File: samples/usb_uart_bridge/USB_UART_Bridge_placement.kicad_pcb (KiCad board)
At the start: 2 copper layers, 68 x 73 mm, 5 parts, among them J1 USB-C, U1 TLV75518, U2 CYUSB3014

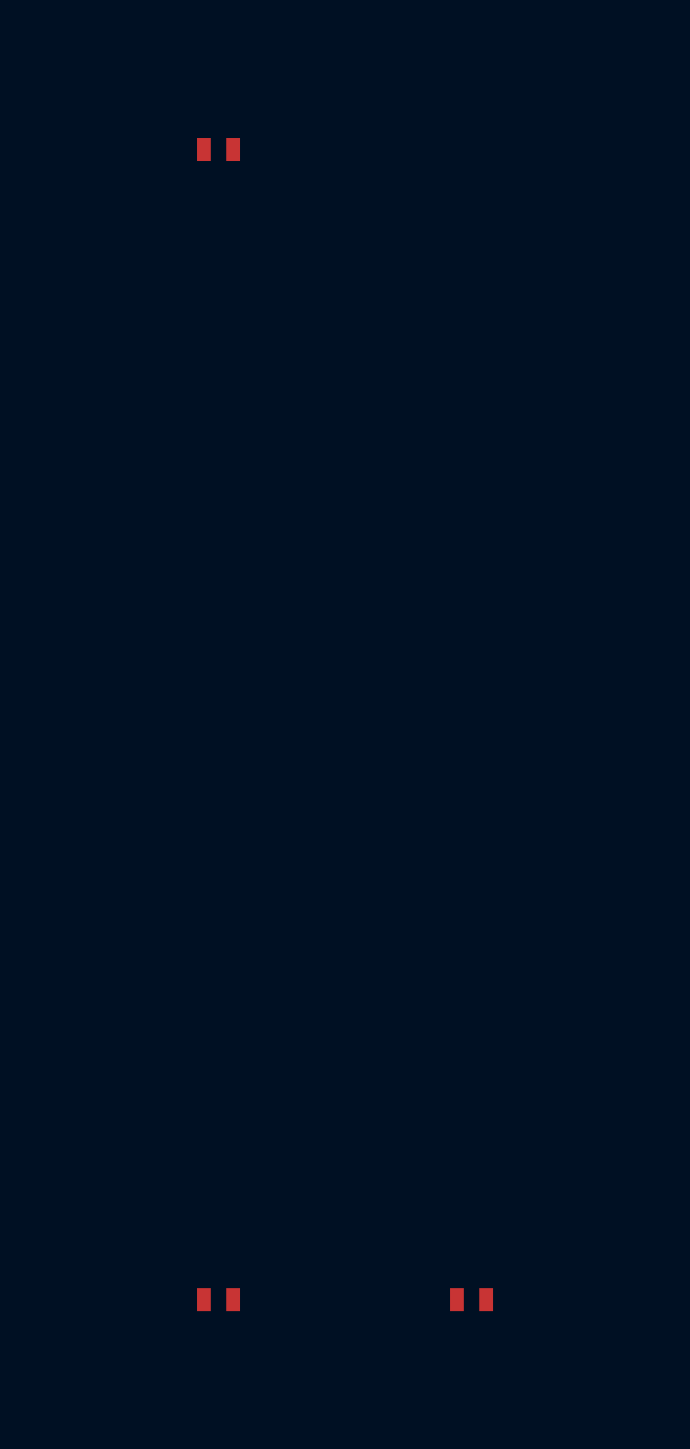
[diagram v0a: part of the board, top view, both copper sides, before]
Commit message: chore: regenerate 8 sample designs against v0.27.0 engine
All 8 samples pass full validation (0 ERC errors):
- led_power_indicator, iot_sensor_node, usb_regulated_supply,
  usb_uart_bridge, oled_display_module, battery_iot_sensor,
  motor_controller, fpga_power_carrier

New artifacts per sample: .kicad_sch, _test_points.csv, _pinout.csv,
canonical_spec.yaml, design_ir.json, validation_report.json; MCU samples
also emit sdkconfig.defaults / .ioc stubs.

Also adds samples/*/svg/ to .gitignore — schematic SVG exports are
regenerable and too large to track.

zigbee_humidistat deferred: non-deterministic schematic output across
two generation runs (text annotation ordering vs sheet_instances).
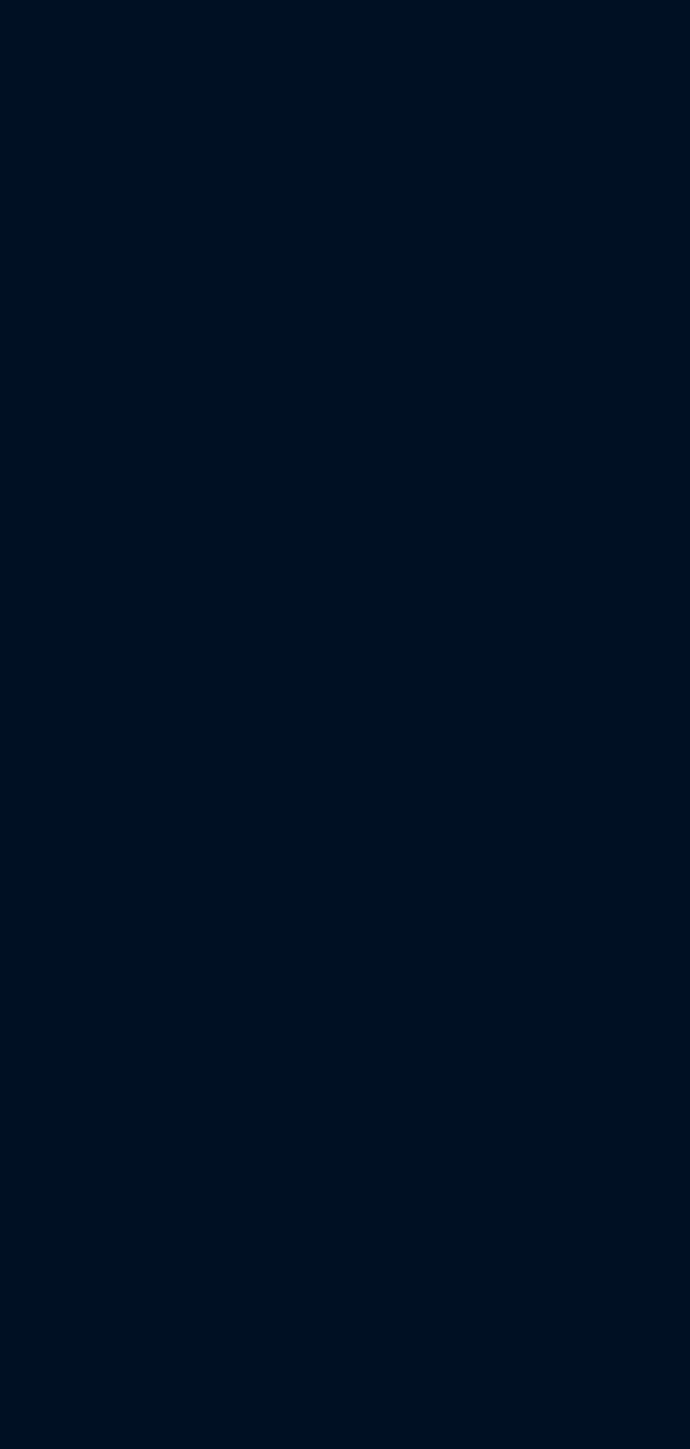
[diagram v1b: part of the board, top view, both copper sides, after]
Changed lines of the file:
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@@
-(kicad_pcb (version 20240108) (generator "schematic_engine")
+(kicad_pcb (version 20240108) (generator "schematic_engine placement_preview")
   (general (thickness 1.6) (legacy_teardrops no))
   (layers
@@
       (effects (font (size 1.0 1.0) (thickness 0.15)))
     )
-    (pad "1" smd rect (at 0.00 0) (size 0.6 1.0) (layers "F.Cu" "F.Paste" "F.Mask") (net 25 "VBUS_5V"))
-    (pad "2" smd rect (at 1.27 0) (size 0.6 1.0) (layers "F.Cu" "F.Paste" "F.Mask") (net 3 "GND"))
   )
   (footprint "Diode_SMD:D_SMB"
@@
       (effects (font (size 1.0 1.0) (thickness 0.15)))
     )
-    (pad "1" smd rect (at 0.00 0) (size 0.6 1.0) (layers "F.Cu" "F.Paste" "F.Mask") (net 26 "VDD"))
-    (pad "2" smd rect (at 1.27 0) (size 0.6 1.0) (layers "F.Cu" "F.Paste" "F.Mask") (net 2 "DVDDIO"))
   )
   (footprint "Connector_USB:USB_C_Receptacle_GCT_USB4085"
@@
       (effects (font (size 1.0 1.0) (thickness 0.15)))
     )
-    (pad "1" smd rect (at 0.00 0) (size 0.6 1.0) (layers "F.Cu" "F.Paste" "F.Mask") (net 25 "VBUS_5V"))
-    (pad "2" smd rect (at 1.27 0) (size 0.6 1.0) (layers "F.Cu" "F.Paste" "F.Mask") (net 3 "GND"))
   )
   (gr_line (start 0.00 0.00) (end 68.00 0.00) (stroke (width 0.1) (type solid)) (layer "Edge.Cuts"))
